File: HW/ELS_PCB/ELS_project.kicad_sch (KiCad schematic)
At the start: 47 parts, among them CN1 JL212V-SMT-35006BP1, CN2 JL212V-SMT-35008BP1, J3 Conn_01x04_Pin, Q1 2N7002, Q2 2N7002, Q3 2N7002, Q4 2N7002, U2 INA180A1, U3 JL212V-SMT-35003BP1, U4 JL212V-SMT-35003BP1

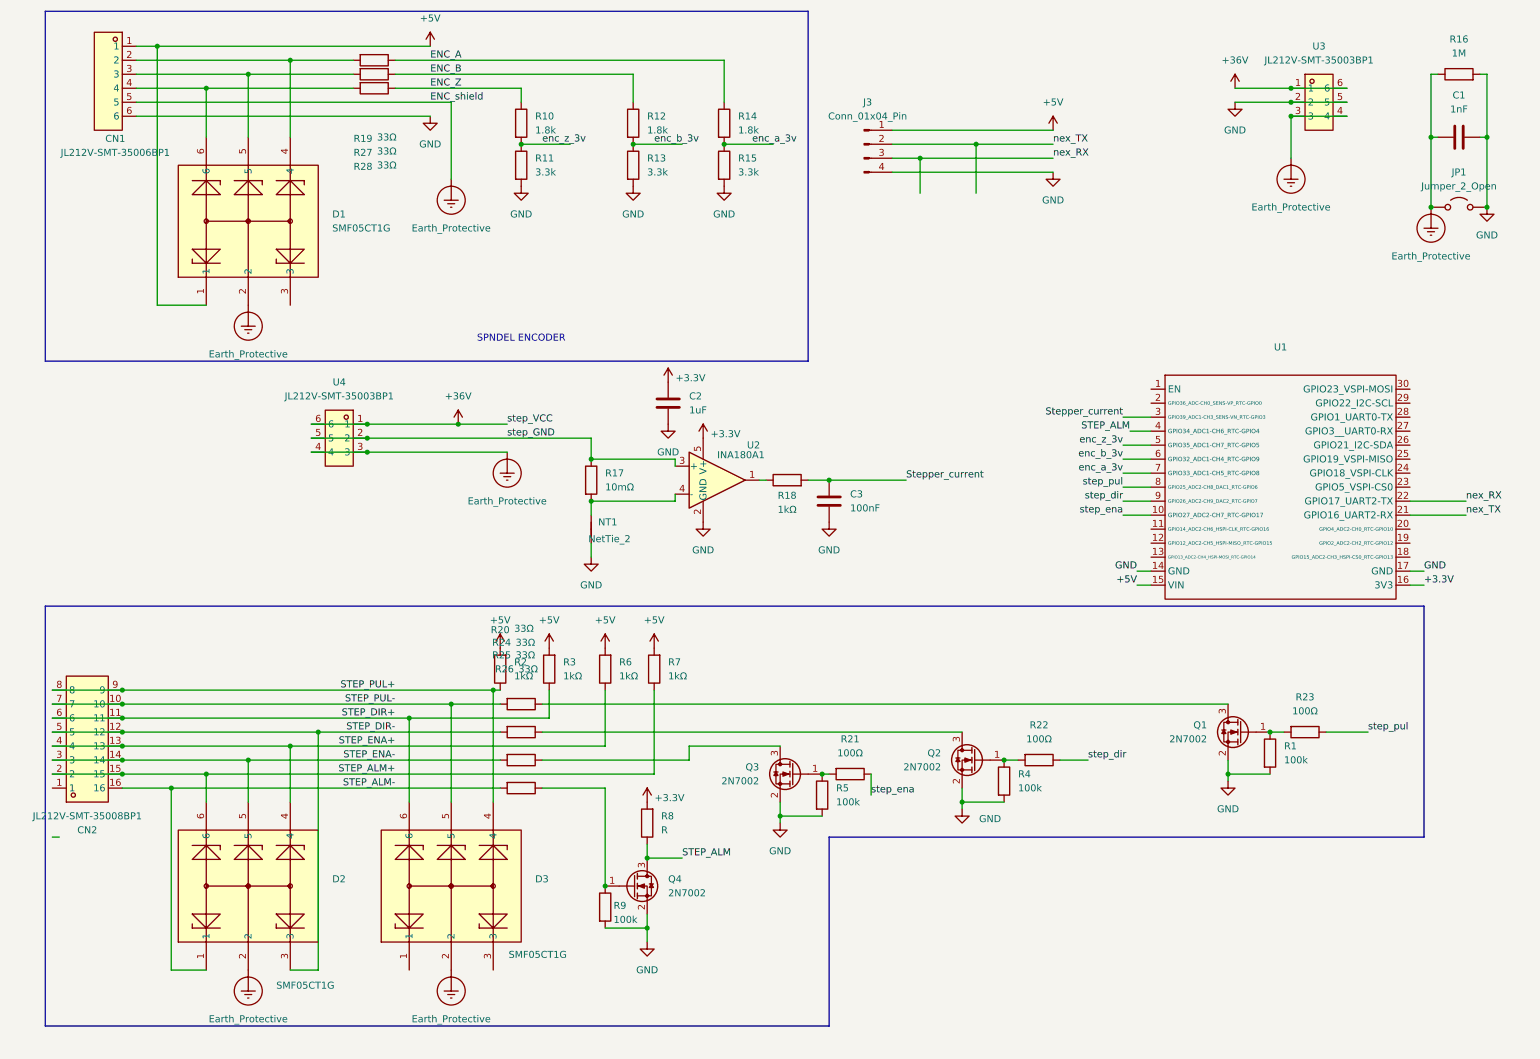
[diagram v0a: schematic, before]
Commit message: redesigned the powerstage sinse the org got realy hot. using newer parts
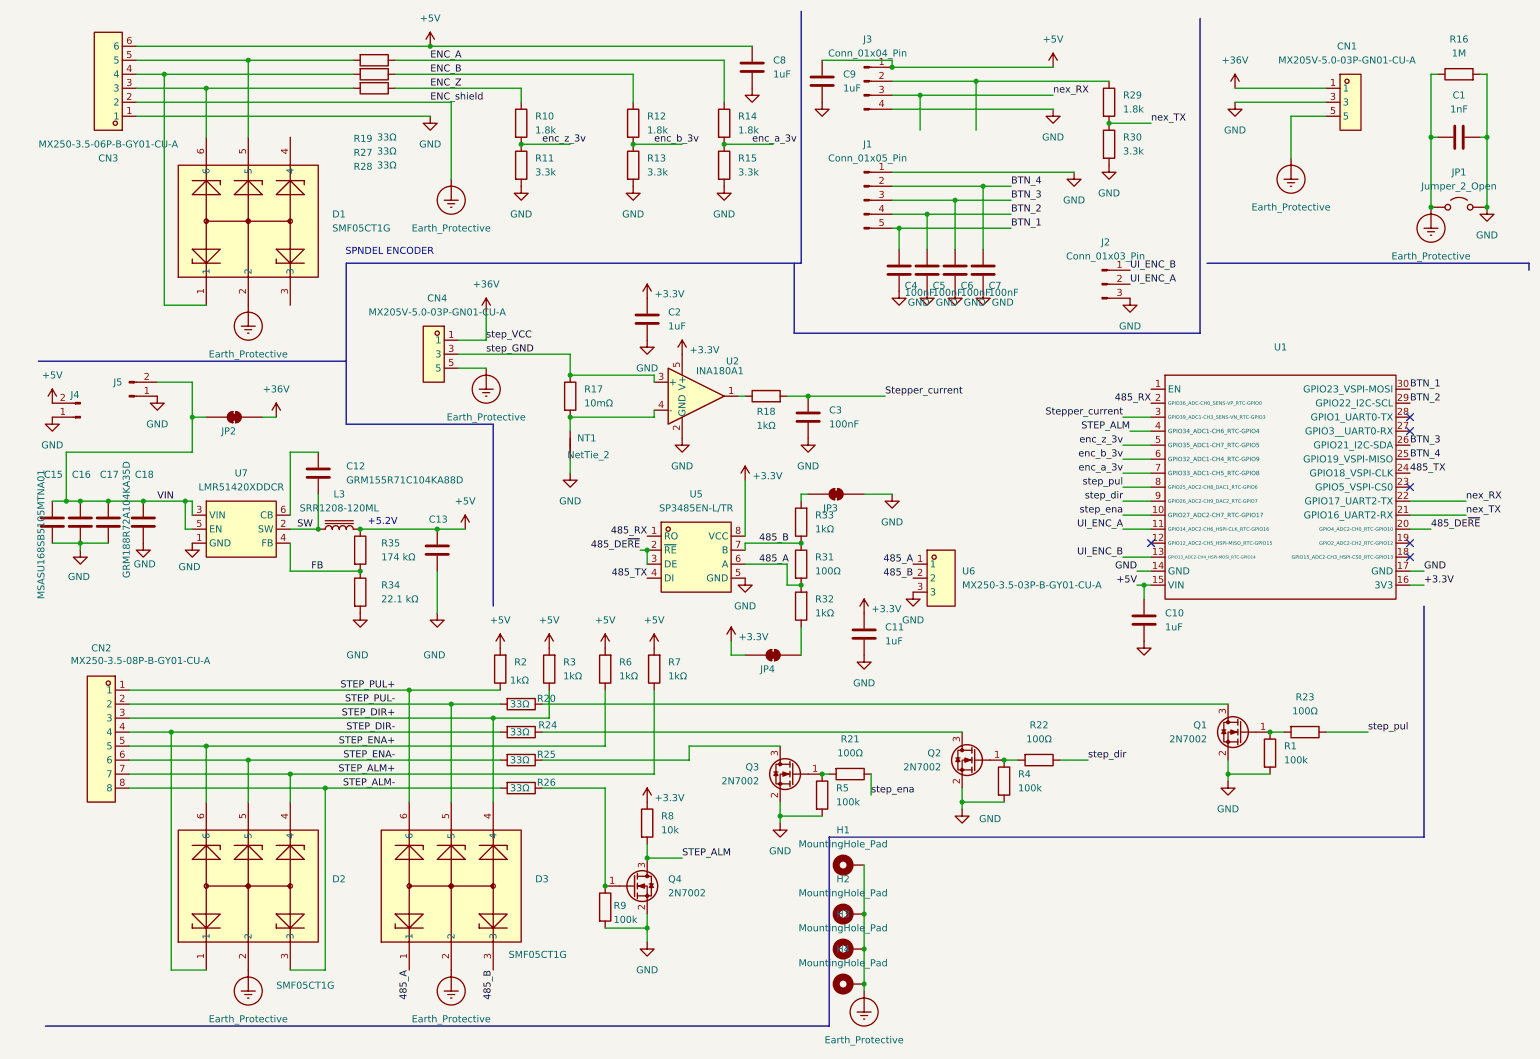
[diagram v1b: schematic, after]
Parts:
- removed CN1: JL212V-SMT-35006BP1, LCSC:CONN-SMD_6P-P3.50_JL212V-SMT-35006BP1, symbol LCSC:JL212V-SMT-35006BP1
- removed CN2: JL212V-SMT-35008BP1, LCSC:CONN-SMD_JL212V-SMT-35008BP1, symbol LCSC:JL212V-SMT-35008BP1
- removed U3, U4: JL212V-SMT-35003BP1, LCSC:CONN-SMD_JL212V-SMT-35003BP1, symbol LCSC:JL212V-SMT-35003BP1
- added C10, C11, C8, C9: 1uF, Capacitor_SMD:C_0402_1005Metric, symbol Device:C
- added C12: GRM155R71C104KA88D, Capacitor_SMD:C_0402_1005Metric, symbol Device:C
- added C13: GRM32ER61C476KE15L, Capacitor_SMD:C_1210_3225Metric, symbol Device:C
- added C15, C16, C17: MSASU168SB5105MTNA01, Capacitor_SMD:C_0603_1608Metric, symbol Device:C
- added C18: GRM188R72A104KA35D, Capacitor_SMD:C_0603_1608Metric, symbol Device:C
- added C4, C5, C6, C7: 100nF, Capacitor_SMD:C_0402_1005Metric, symbol Device:C
- added CN1, CN4: MX205V-5.0-03P-GN01-CU-A, LCSC:CONN-TH_3P-P5.00_MX205V-5.0-03P-GN01-CU-A, symbol LCSC:MX205V-5.0-03P-GN01-CU-A
- added CN2: MX250-3.5-08P-B-GY01-CU-A, LCSC:CONN-TH_8P-P3.50-LS5.10_MX250-3.5-08P-B-GY01-CU-A, symbol LCSC:MX250-3.5-08P-B-GY01-CU-A
- added CN3: MX250-3.5-06P-B-GY01-CU-A, LCSC:CONN-TH_6P-P3.50_MX250-3.5-06P-B-GY01-CU-A, symbol LCSC:MX250-3.5-06P-B-GY01-CU-A
- added H1, H2, H3, H4: MountingHole_Pad, MountingHole:MountingHole_3.2mm_M3_Pad_TopOnly, symbol Mechanical:MountingHole_Pad
- added J1: Conn_01x05_Pin, Connector_JST:JST_PH_B5B-PH-K_1x05_P2.00mm_Vertical, symbol Connector:Conn_01x05_Pin
- added J2: Conn_01x03_Pin, Connector_JST:JST_PH_B3B-PH-K_1x03_P2.00mm_Vertical, symbol Connector:Conn_01x03_Pin
- added J4, J5: Conn_01x02_Pin, Connector_JST:JST_XH_B2B-XH-AM_1x02_P2.50mm_Vertical, symbol Connector:Conn_01x02_Pin
- added JP2, JP3, JP4: SolderJumper_2_Bridged, Jumper:SolderJumper-2_P1.3mm_Bridged_Pad1.0x1.5mm, symbol Jumper:SolderJumper_2_Bridged
- added L3: SRR1208-120ML, Inductor_SMD:L_Bourns_SRR1208_12.7x12.7mm, symbol Device:L_Iron
- added R29: 1.8k, Resistor_SMD:R_0603_1608Metric, symbol Device:R
- added R30: 3.3k, Resistor_SMD:R_0603_1608Metric, symbol Device:R
- added R31: 100Ω, Resistor_SMD:R_0402_1005Metric, symbol Device:R
- added R32, R33: 1kΩ, Resistor_SMD:R_0603_1608Metric, symbol Device:R
- added R34: 22.1 kΩ, Resistor_SMD:R_0402_1005Metric, symbol Device:R
- added R35: 174 kΩ, Resistor_SMD:R_0402_1005Metric, symbol Device:R
- added U5: SP3485EN-L/TR, LCSC:SOIC-8_L5.0-W4.0-P1.27-LS6.0-BL, symbol LCSC:SP3485EN-L_TR
- added U6: MX250-3.5-03P-B-GY01-CU-A, LCSC:CONN-TH_3P-P3.50_MX250-3.5-03P-B-GY01-CU-A, symbol LCSC:MX250-3.5-03P-B-GY01-CU-A
- added U7: LMR51420XDDCR, LCSC:SOT-23-6_L2.9-W1.6-P0.95-LS2.8-BL, symbol LCSC:LMR51420XDDCR
- D1, D2, D3: LCSC C15879 -> (none)
- J3: footprint (none) -> Connector_JST:JST_PH_B4B-PH-K_1x04_P2.00mm_Vertical; now left out of the parts list
- JP1: now left out of the parts list
- R8: value R -> 10k; LCSC (none) -> C25803
- U1: value ~ -> (none)
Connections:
- net +3.3V: now also R8.1, C11.2, JP4.2 (B), U5.8 (VCC); no longer R8.2
- net +36V: now also CN1.1, CN1.2, CN4.1, CN4.2, JP2.1 (A)
- net +5V: now also C10.2, C13.1, C8.2, C9.2, CN3.6, J4.2 (Pin_2), L3.2, R35.1; no longer D1.1
- net Earth_Protective: now also CN1.5, CN1.6, CN3.2, CN4.5, CN4.6, H1.1, H2.1, H3.1, H4.1
- net GND: now also C10.1, C11.1, C13.2, C15.2, C16.2, C17.2, C18.2, C4.1, C5.1, C6.1, C7.1, C8.1, C9.1, CN1.3, CN1.4, CN3.1, J1.1 (Pin_1), J2.3 (Pin_3), J4.1 (Pin_1), J5.1 (Pin_1), JP3.1 (A), R30.2, R34.2, U5.5 (GND), U6.3, U7.1 (GND)
- net STEP_ALM: now also R8.2; no longer R8.1
- net STEP_ALM+: now also D2.4, CN2.7; no longer D2.6
- net STEP_ALM-: now also D2.3, CN2.8; no longer D2.1
- net STEP_DIR+: now also D3.4, CN2.3; no longer D3.6
- net STEP_DIR-: now also D2.1, CN2.4; no longer D2.3
- net STEP_ENA+: now also D2.6, CN2.5; no longer D2.4
- net STEP_ENA-: now also CN2.6
- net STEP_PUL+: now also D3.6, CN2.1; no longer D3.4
- net STEP_PUL-: now also CN2.2
- net nex_TX: now also R29.2, R30.1; no longer J3.2 (Pin_2)
- net step_GND: now also CN4.3, CN4.4
- net at D1.4: no longer R19.2
- net at R27.2: now also D1.1, CN3.4; no longer D1.5
- net at D1.6, R28.2: now also CN3.3
- net UI_ENC_A: now reaches U1.11 (GPIO14_ADC2-CH6_HSPI-CLK_RTC-GPIO16)
- net UI_ENC_A: now also J2.2 (Pin_2)
- net UI_ENC_B: now reaches U1.13 (GPIO13_ADC2-CH4_HSPI-MOSI_RTC-GPIO14)
- net UI_ENC_B: now also J2.1 (Pin_1)
- net 485_RX: now reaches U1.2 (GPIO36_ADC-CH0_SENS-VP_RTC-GPIO0)
- net 485_RX: now also U5.1 (RO)
- net 485_DE~{RE}: now reaches U1.20 (GPIO4_ADC2-CH0_RTC-GPIO10)
- net 485_DE~{RE}: now also U5.2 (~{RE}), U5.3 (DE)
- net 485_TX: now reaches U1.24 (GPIO18_VSPI-CLK)
- net 485_TX: now also U5.4 (DI)
- net BTN_4: now reaches U1.25 (GPIO19_VSPI-MISO)
- net BTN_4: now also C7.2, J1.2 (Pin_2)
- net BTN_3: now reaches U1.26 (GPIO21_I2C-SDA)
- net BTN_3: now also C6.2, J1.3 (Pin_3)
- net BTN_2: now reaches U1.29 (GPIO22_I2C-SCL)
- net BTN_2: now also C5.2, J1.4 (Pin_4)
- net BTN_1: now reaches U1.30 (GPIO23_VSPI-MOSI)
- net BTN_1: now also C4.2, J1.5 (Pin_5)
- net 485_A: now reaches D3.1
- net 485_A: now also R31.2, R32.2, U5.6 (A), U6.1
- net 485_B: now reaches D3.3
- net 485_B: now also R31.1, R33.1, U5.7 (B), U6.2
- new net: J3.2 (Pin_2), R29.1
- new net: JP3.2 (B), R33.2
- new net: CN3.5, D1.5, R19.2
- new net: C12.1, U7.6 (CB)
- new net: JP4.1 (A), R32.1
- new net FB: R34.1, R35.2, U7.4 (FB)
- new net SW: C12.2, L3.1, U7.2 (SW)
- new net VIN: C15.1, C16.1, C17.1, C18.1, J5.2 (Pin_2), JP2.2 (B), U7.3 (VIN), U7.5 (EN)
- no-connect marks 0 -> 6
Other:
- note added: "+5.2V"
- moved on the sheet: C2, C3, J3, NT1, R17, R18, U2
